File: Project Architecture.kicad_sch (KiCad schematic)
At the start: 0 parts

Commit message: Frist draft of Schematic
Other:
- removed sheet Section A - Title A
- removed sheet Section B - Title B
- added sheet CH552G (CH552G.kicad_sch)
- added sheet USB (USB.kicad_sch)
- added sheet ws2128S (ws2128S.kicad_sch)
- note removed: "Page 4"
- note removed: "Page 5"

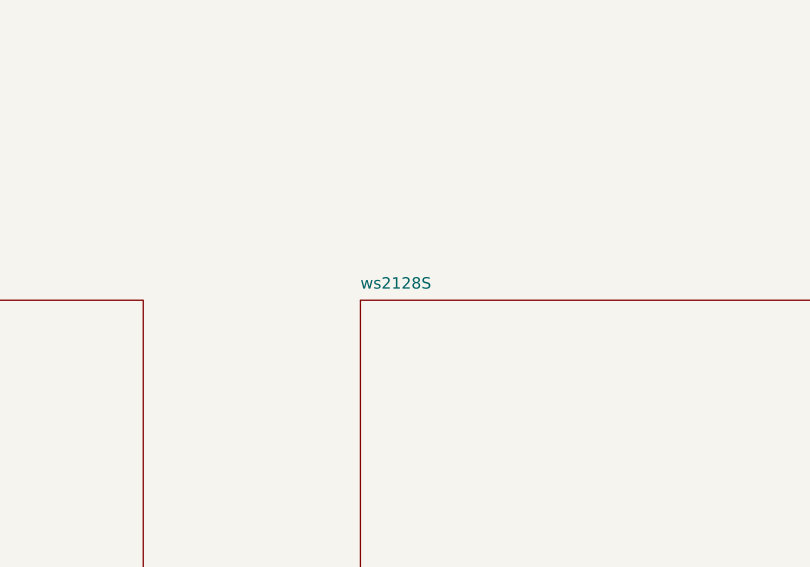
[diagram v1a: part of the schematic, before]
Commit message: updated titles and changes to wires
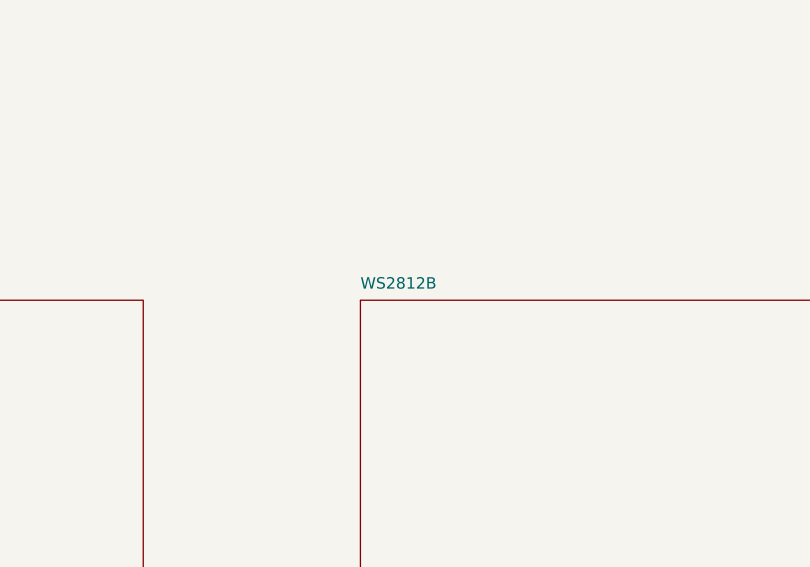
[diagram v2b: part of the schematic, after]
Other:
- sheet ws2128S renamed WS2812B
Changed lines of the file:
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@@
 			(color 255 229 191 1.0000)
 		)
-		(property "Sheetname" "ws2128S"
+		(property "Sheetname" "WS2812B"
 			(at 279.4 75.0646 0)
 			(effects

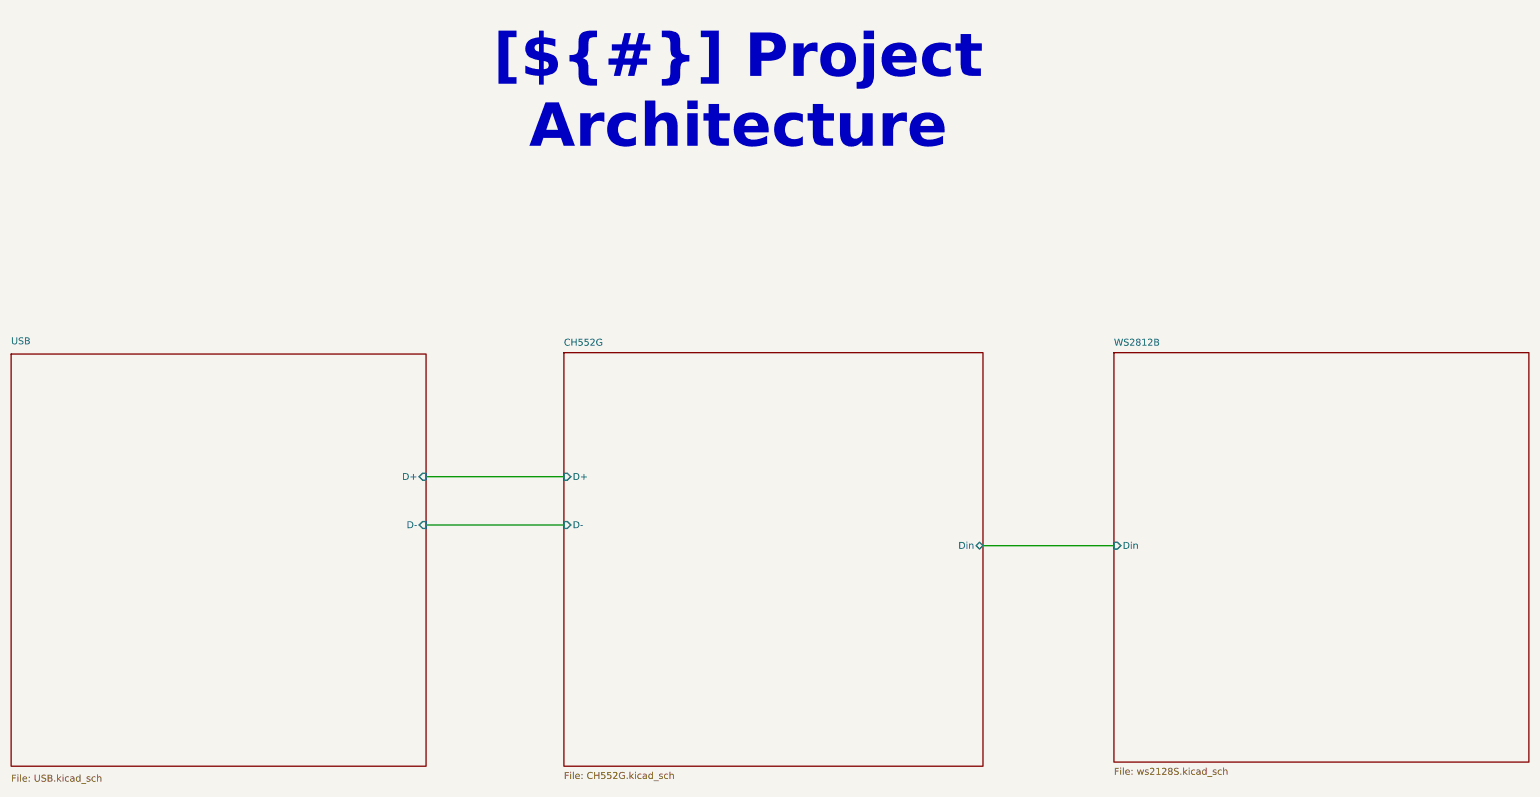
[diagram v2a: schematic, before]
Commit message: updated titles and changes to wires
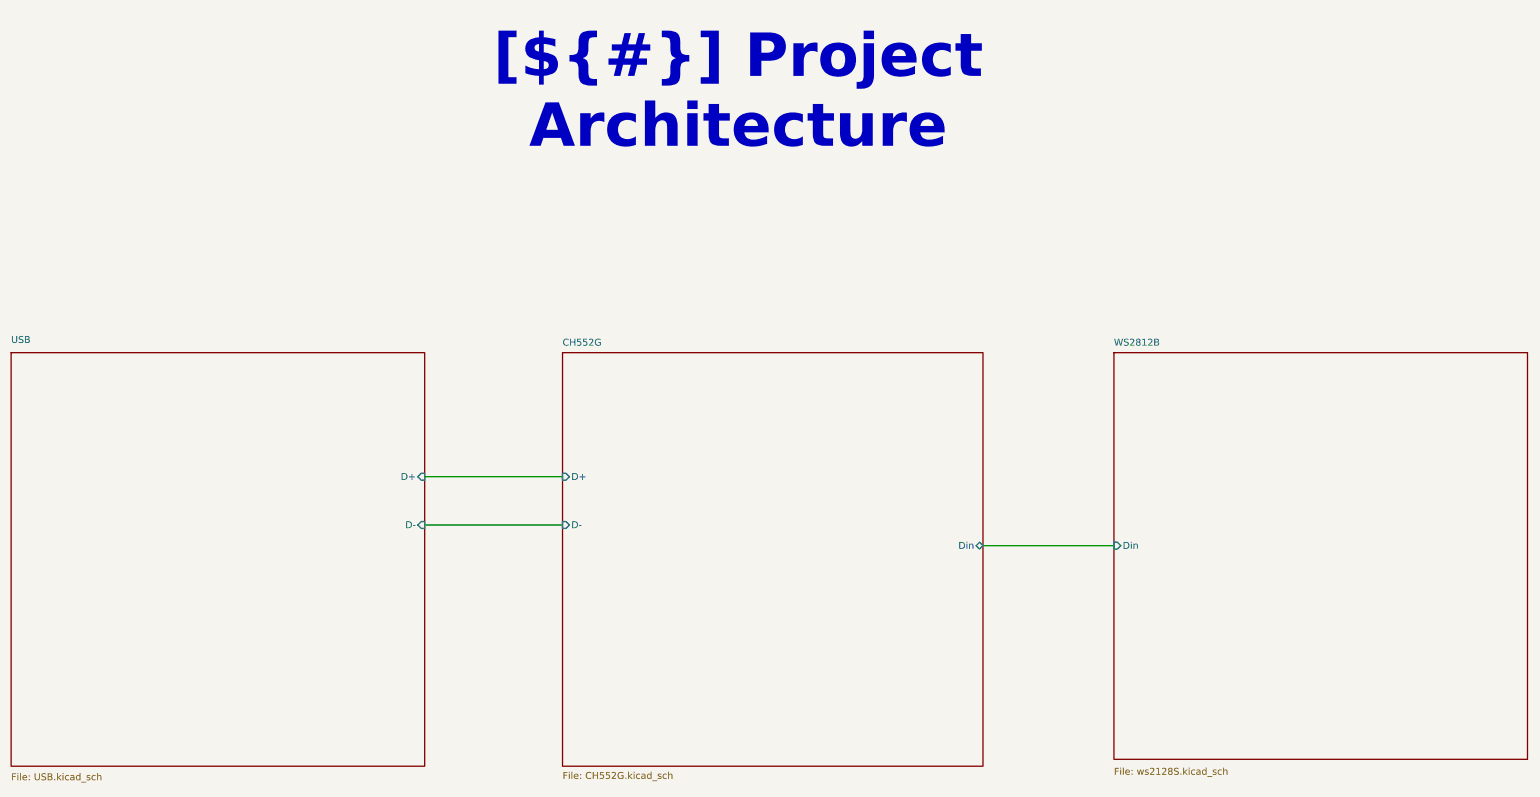
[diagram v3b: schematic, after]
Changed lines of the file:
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@@
+	(wire
+		(pts
+			(xy 152.4 99.06) (xy 177.8 99.06)
+		)
+		(stroke
+			(width 0)
+			(type default)
+		)
+	)
+	(wire
+		(pts
+			(xy 152.4 107.95) (xy 177.8 107.95)
+		)
+		(stroke
+			(width 0)
+			(type default)
+		)
+	)
 	(wire
 		(pts
@@
 		)
 	)
-	(wire
-		(pts
-			(xy 152.654 99.06) (xy 178.054 99.06)
-		)
-		(stroke
-			(width 0)
-			(type default)
-		)
-	)
-	(wire
-		(pts
-			(xy 152.654 107.95) (xy 178.054 107.95)
-		)
-		(stroke
-			(width 0)
-			(type default)
-		)
-	)
 	(sheet
-		(at 178.054 76.2)
-		(size 77.216 76.2)
+		(at 177.8 76.2)
+		(size 77.47 76.2)
 		(exclude_from_sim no)
 		(in_bom yes)
@@
 		)
 		(property "Sheetname" "CH552G"
-			(at 178.054 75.0646 0)
+			(at 177.8 75.0646 0)
 			(effects
 				(font
@@
 		)
 		(property "Sheetfile" "CH552G.kicad_sch"
-			(at 178.054 153.4084 0)
+			(at 177.8 153.4084 0)
 			(effects
 				(font
@@
 		)
 		(pin "D+" input
-			(at 178.054 99.06 180)
+			(at 177.8 99.06 180)
 			(effects
 				(font
@@
 		)
 		(pin "D-" input
-			(at 178.054 107.95 180)
+			(at 177.8 107.95 180)
 			(effects
 				(font
@@
 	)
 	(sheet
-		(at 76.2 76.454)
-		(size 76.454 75.946)
+		(at 76.2 76.2)
+		(size 76.2 76.2)
 		(exclude_from_sim no)
 		(in_bom yes)
@@
 		)
 		(property "Sheetname" "USB"
-			(at 76.2 74.8186 0)
+			(at 76.2 74.5646 0)
 			(effects
 				(font
@@
 		)
 		(property "Sheetfile" "USB.kicad_sch"
-			(at 76.2 153.9084 0)
+			(at 76.2 153.6544 0)
 			(effects
 				(font
@@
 		)
 		(pin "D+" input
-			(at 152.654 99.06 0)
+			(at 152.4 99.06 0)
 			(effects
 				(font
@@
 		)
 		(pin "D-" input
-			(at 152.654 107.95 0)
+			(at 152.4 107.95 0)
 			(effects
 				(font
@@
 	(sheet
 		(at 279.4 76.2)
-		(size 76.454 75.438)
+		(size 76.2 74.93)
 		(exclude_from_sim no)
 		(in_bom yes)
